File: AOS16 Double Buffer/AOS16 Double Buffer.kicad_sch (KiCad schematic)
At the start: 4 parts, among them IC1 SN74AUP2G14DCKR, J1 Conn_01x07_Pin, U1 74LS157, U2 74LS157

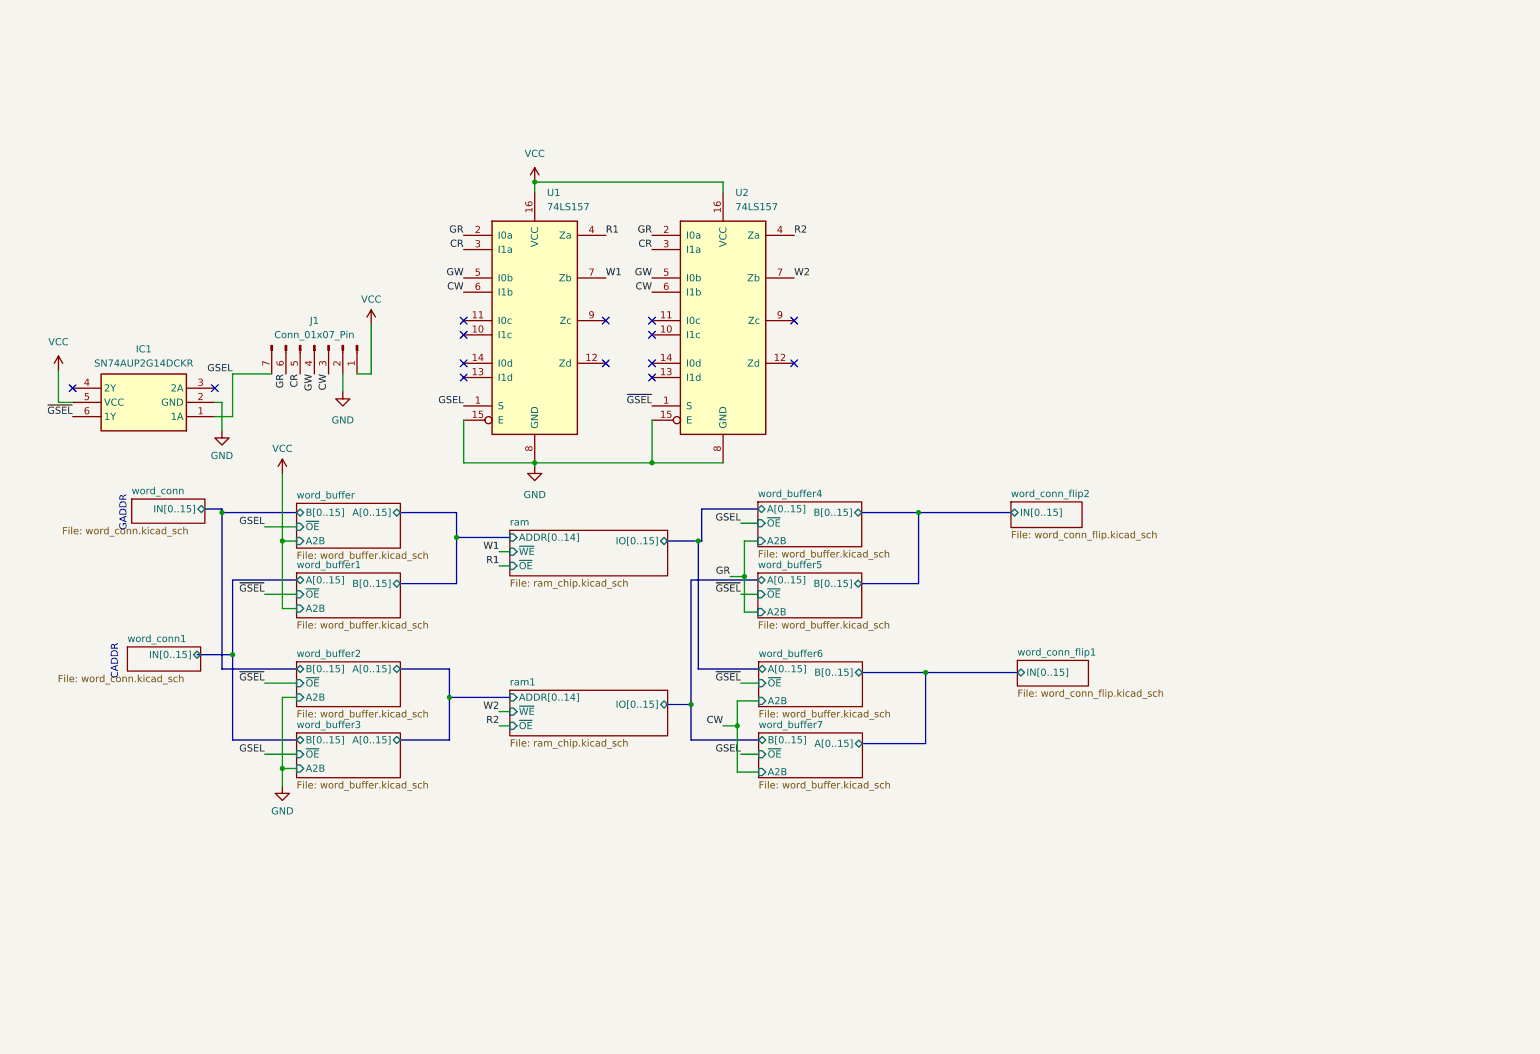
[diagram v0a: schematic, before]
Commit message: updated double buffer
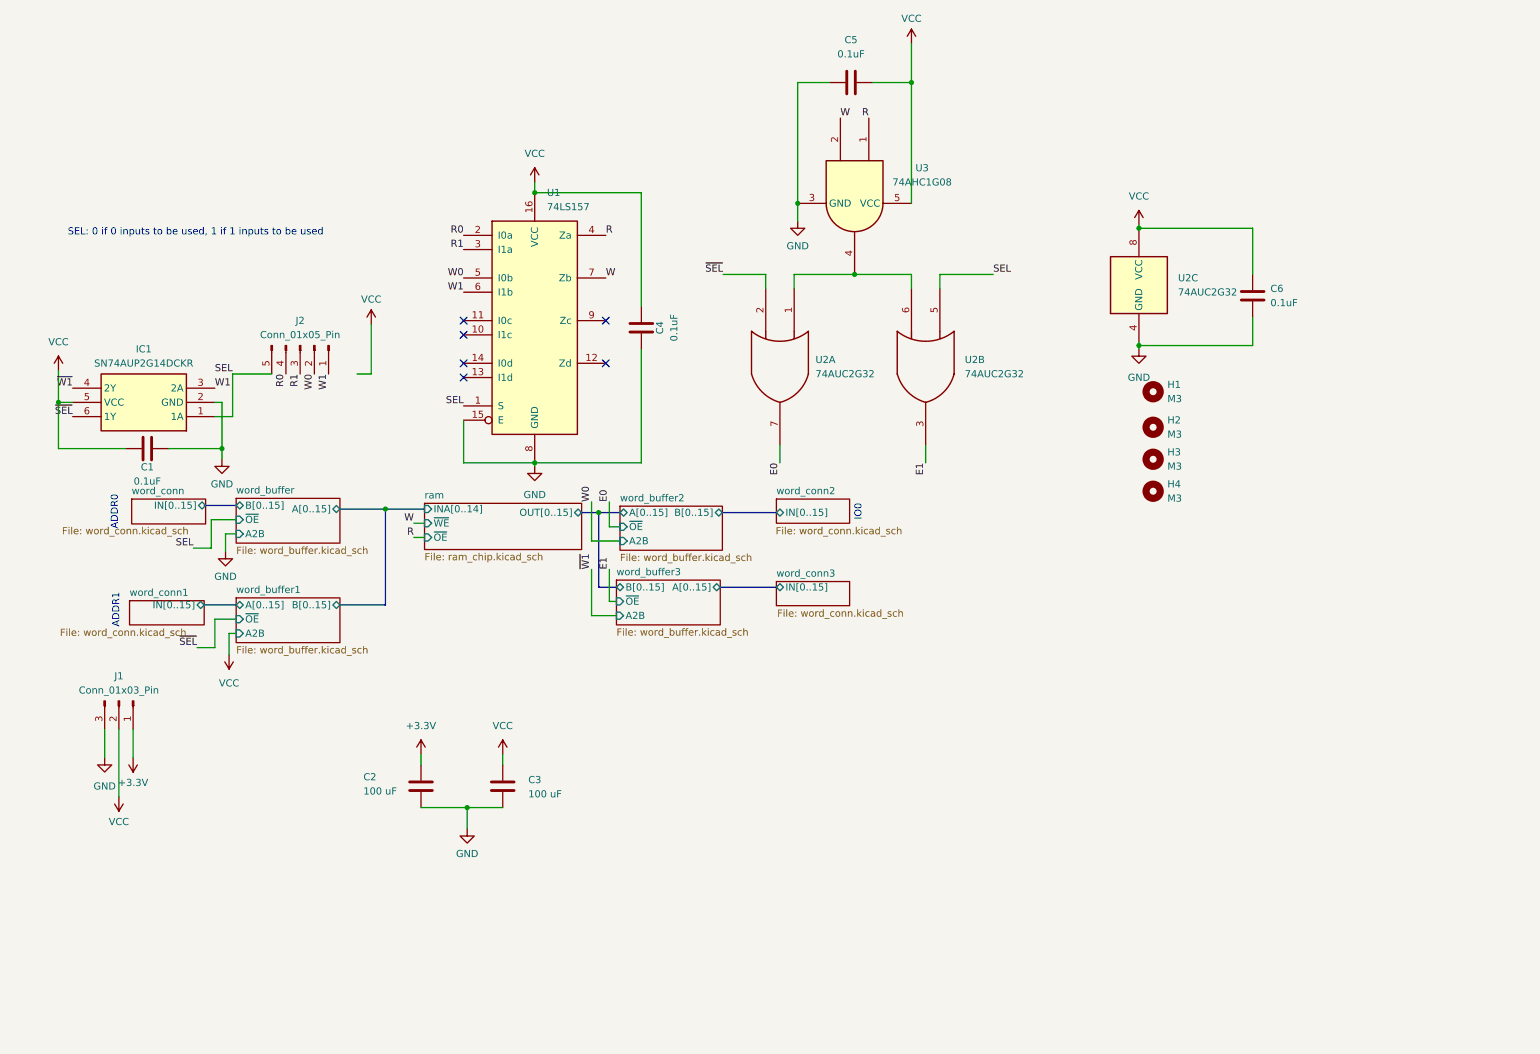
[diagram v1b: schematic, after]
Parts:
- removed J1: Conn_01x07_Pin, Connector_PinSocket_2.54mm:PinSocket_1x07_P2.54mm_Vertical, symbol Connector:Conn_01x07_Pin
- removed U2: 74LS157, Package_SO:SOIC-16_3.9x9.9mm_P1.27mm, symbol 74xx:74LS157
- added C1, C4, C5, C6: 0.1uF, Capacitor_SMD:C_0603_1608Metric, symbol Device:C
- added C2, C3: 100 uF, Capacitor_SMD:CP_Elec_5x5.3, symbol Device:C
- added H1, H2, H3, H4: M3, MountingHole:MountingHole_3.2mm_M3, symbol Mechanical:MountingHole
- added J1: Conn_01x03_Pin, Connector_PinHeader_2.54mm:PinHeader_1x03_P2.54mm_Vertical, symbol Connector:Conn_01x03_Pin
- added J2: Conn_01x05_Pin, Connector_PinHeader_2.54mm:PinHeader_1x05_P2.54mm_Vertical, symbol Connector:Conn_01x05_Pin
- added U2: 74AUC2G32, Package_SO:SSOP-8_2.95x2.8mm_P0.65mm, symbol 74xGxx:74AUC2G32
- added U3: 74AHC1G08, Package_TO_SOT_SMD:SOT-23-5, symbol 74xGxx:74AHC1G08
- IC1: footprint sn74aup2:SOT65P210X110-6N -> Package_TO_SOT_SMD:SOT-363_SC-70-6
- U1: Manufacturer_Part_Number (none) -> SN74LS157
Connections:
- net CR is gone; now on net R1: U1.3 (I1a)
- net CW is gone; now on net W1: U1.6 (I1b)
- net GND: now also C1.2, C2.2, C3.2, C4.1, C5.1, C6.2, J1.3 (Pin_3), U2.4 (GND), U3.3 (GND)
- net R1: now also J2.3 (Pin_3); no longer U1.4 (Za)
- net VCC: now also C1.1, C3.1, C4.2, C5.2, C6.1, J1.2 (Pin_2), U2.8 (VCC), U3.5 (VCC)
- net W1: now also IC1.3 (2A), J2.1 (Pin_1); no longer U1.7 (Zb)
- net ~{W1}: now reaches IC1.4 (2Y)
- net GR renamed R0
- net R0: now also J2.4 (Pin_4)
- net GSEL renamed SEL
- net SEL: now also J2.5 (Pin_5), U2.5
- net GW renamed W0
- net W0: now also J2.2 (Pin_2)
- net ~{GSEL} renamed ~{SEL}
- net ~{SEL}: now also U2.2
- new net: U2.1, U2.6, U3.4
- new net +3.3V: C2.1, J1.1 (Pin_1)
- new net E0: U2.7
- new net E1: U2.3
- new net R: U1.4 (Za), U3.1
- new net W: U1.7 (Zb), U3.2
- no-connect marks 14 -> 6
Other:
- removed sheet ram1
- removed sheet word_buffer4
- removed sheet word_buffer5
- removed sheet word_buffer6
- removed sheet word_buffer7
- removed sheet word_conn_flip1
- removed sheet word_conn_flip2
- added sheet word_conn2 (word_conn.kicad_sch)
- added sheet word_conn3 (word_conn.kicad_sch)
- sheet ram ports: added INA[0..14], OUT[0..15]; removed ADDR[0..14], IO[0..15]
- note added: "ADDR0"
- note added: "ADDR1"
- note added: "IO0"
- note added: "SEL: 0 if 0 inputs to be used, 1 if 1 inputs to be used"
- note removed: "CADDR"
- note removed: "GADDR"

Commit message: Completed double buffer first draft
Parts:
- removed C4: 0.1uF, Capacitor_SMD:C_0603_1608Metric, symbol Device:C
- removed H1, H2, H3, H4: M3, MountingHole:MountingHole_3.2mm_M3, symbol Mechanical:MountingHole
- removed IC1: SN74AUP2G14DCKR, Package_TO_SOT_SMD:SOT-363_SC-70-6, symbol SN74AUP2G14DCKR:SN74AUP2G14DCKR
- removed J1: Conn_01x03_Pin, Connector_PinHeader_2.54mm:PinHeader_1x03_P2.54mm_Vertical, symbol Connector:Conn_01x03_Pin
- removed J2: Conn_01x05_Pin, Connector_PinHeader_2.54mm:PinHeader_1x05_P2.54mm_Vertical, symbol Connector:Conn_01x05_Pin
- removed U1: 74LS157, Package_SO:SOIC-16_3.9x9.9mm_P1.27mm, symbol 74xx:74LS157
- removed U2: 74AUC2G32, Package_SO:SSOP-8_2.95x2.8mm_P0.65mm, symbol 74xGxx:74AUC2G32
- removed U3: 74AHC1G08, Package_TO_SOT_SMD:SOT-23-5, symbol 74xGxx:74AHC1G08
- added C2, C7, C8, C9: 0.1uF, Capacitor_SMD:C_0603_1608Metric, symbol Device:C
- added J1: Conn_01x02_Pin, Connector_PinHeader_2.54mm:PinHeader_1x02_P2.54mm_Vertical, symbol Connector:Conn_01x02_Pin
- added J6: Conn_01x07_Pin, Connector_PinHeader_2.54mm:PinHeader_1x07_P2.54mm_Vertical, symbol Connector:Conn_01x07_Pin
- added U1, U2: 74AHC1G08, Package_TO_SOT_SMD:SOT-353_SC-70-5, symbol 74xGxx:74AHC1G08
- added U3, U4: 74AHC1G32, Package_TO_SOT_SMD:SOT-353_SC-70-5, symbol 74xGxx:74AHC1G32
- added U5, U6: 74AHC1G04, Package_TO_SOT_SMD:SOT-353_SC-70-5, symbol 74xGxx:74AHC1G04
- added U7: 74LS157, Package_SO:SOIC-16_3.9x9.9mm_P1.27mm, symbol 74xx:74LS157
- C1, C5, C6: Manufacturer_Part_Number CL10B104KO8WPNL -> (none)
- renumbered C2 to C3, C3 to C4
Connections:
- net +3.3V: now also J1.1 (Pin_1)
- net E0: now also U3.4
- net E1: now also U4.4
- net GND: now also C5.2, C2.2, C7.2, C8.2, C9.2, J1.2 (Pin_2), J6.7 (Pin_7), U1.3 (GND), U2.3 (GND), U3.3 (GND), U4.3 (GND), U5.3 (GND), U6.3 (GND), U7.15 (E), U7.8 (GND); no longer C5.1
- net R: now also U7.4 (Za)
- net R0: now also J6.4 (Pin_4), U1.1, U7.2 (I0a)
- net R1: now also J6.3 (Pin_3), U2.1, U7.3 (I1a)
- net SEL: now also J6.5 (Pin_5), U3.2, U5.2, U7.1 (S)
- net VCC: now also C5.1, C2.1, C7.1, C8.1, C9.1, J6.6 (Pin_6), U1.5 (VCC), U2.5 (VCC), U3.5 (VCC), U4.5 (VCC), U5.5 (VCC), U6.5 (VCC), U7.16 (VCC); no longer C5.2
- net W: now also U7.7 (Zb)
- net W0: now also J6.2 (Pin_2), U1.2, U7.5 (I0b)
- net W1: now also J6.1 (Pin_1), U2.2, U6.2, U7.6 (I1b)
- net ~{SEL}: now also U4.2, U5.4
- net ~{W1}: now also U6.4
- new net: U2.4, U4.1
- new net: U1.4, U3.1
- no-connect marks 6 -> 0
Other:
- note added: "IO1"
- note removed: "SEL: 0 if 0 inputs to be used, 1 if 1 inputs to be used"

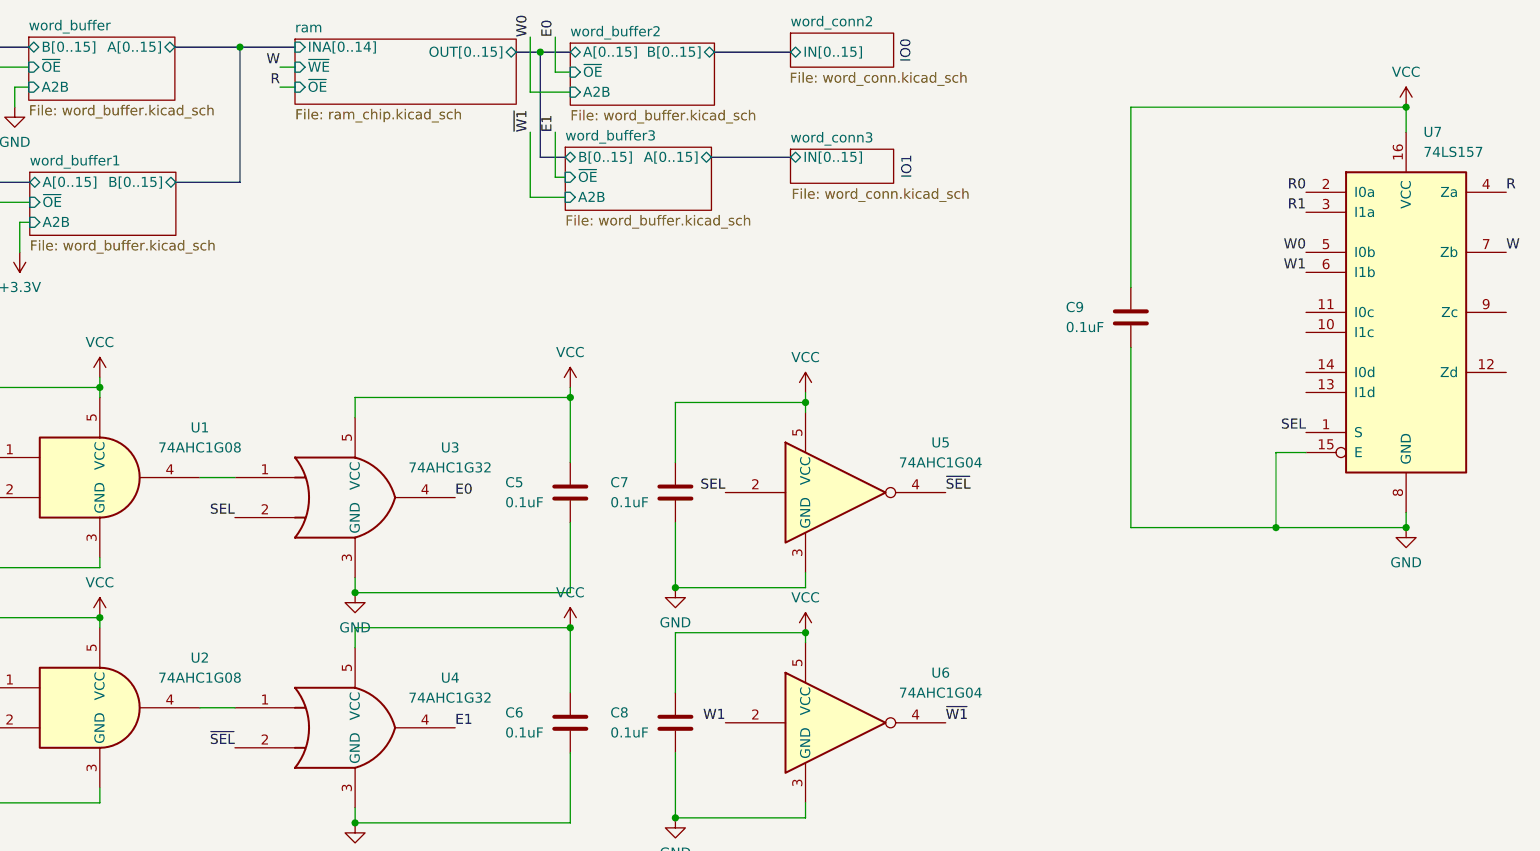
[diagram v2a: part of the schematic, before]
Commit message: Double Buffer Revision
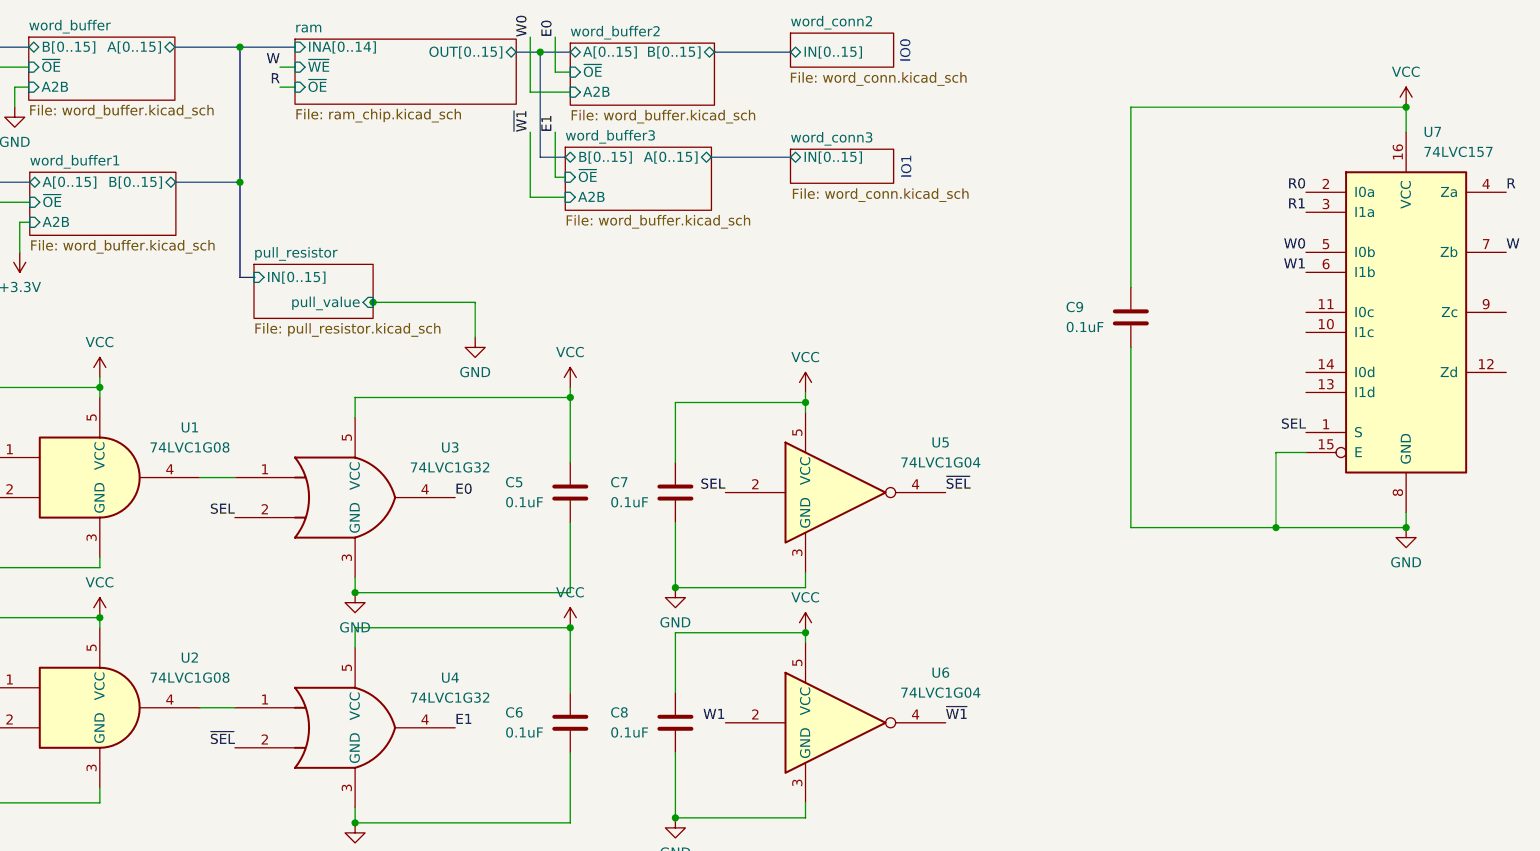
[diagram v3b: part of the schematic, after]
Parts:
- U1, U2: value 74AHC1G08 -> 74LVC1G08
- U3, U4: value 74AHC1G32 -> 74LVC1G32
- U5, U6: value 74AHC1G04 -> 74LVC1G04
- U7: value 74LS157 -> 74LVC157
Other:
- added sheet pull_resistor (pull_resistor.kicad_sch)
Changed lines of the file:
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@@
 	)
 	(junction
+		(at 90.551 53.34)
+		(diameter 0)
+		(color 0 0 0 0)
+	)
+	(junction
 		(at 32.385 86.995)
 		(diameter 0)
@@
 	)
 	(junction
+		(at 73.66 38.1)
+		(diameter 0)
+		(color 0 0 0 0)
+	)
+	(junction
 		(at 111.76 21.59)
 		(diameter 0)
@@
 		)
 	)
+	(bus
+		(pts
+			(xy 73.66 38.1) (xy 73.66 50.165)
+		)
+		(stroke
+			(width 0)
+			(type default)
+		)
+	)
 	(wire
 		(pts
@@
 	(wire
 		(pts
+			(xy 103.505 53.34) (xy 103.505 57.785)
+		)
+		(stroke
+			(width 0)
+			(type default)
+		)
+	)
+	(wire
+		(pts
 			(xy 186.69 59.055) (xy 186.69 81.915)
 		)
@@
 	(wire
 		(pts
+			(xy 90.17 53.34) (xy 90.551 53.34)
+		)
+		(stroke
+			(width 0)
+			(type default)
+		)
+	)
+	(wire
+		(pts
 			(xy 68.58 75.565) (xy 73.025 75.565)
 		)
@@
 		)
 	)
+	(bus
+		(pts
+			(xy 75.565 50.165) (xy 73.66 50.165)
+		)
+		(stroke
+			(width 0)
+			(type default)
+		)
+	)
 	(wire
 		(pts
@@
 	(wire
 		(pts
+			(xy 90.551 53.34) (xy 103.505 53.34)
+		)
+		(stroke
+			(width 0)
+			(type default)
+		)
+	)
+	(wire
+		(pts
 			(xy 55.88 86.995) (xy 55.88 85.725)
 		)
@@
 			)
 		)
-		(property "Value" "74AHC1G32"
+		(property "Value" "74LVC1G32"
 			(at 100.33 103.5364 0)
 			(effects
@@
 			)
 		)
-		(property "Value" "74AHC1G32"
+		(property "Value" "74LVC1G32"
 			(at 100.33 74.3264 0)
 			(effects
@@
 			)
 		)
-		(property "Value" "74LS157"
+		(property "Value" "74LVC157"
 			(at 223.8091 34.29 0)
 			(effects
@@
 			)
 		)
-		(property "Value" "74AHC1G04"
+		(property "Value" "74LVC1G04"
 			(at 162.56 73.6914 0)
 			(effects
@@
 	)
 	(symbol
+		(lib_id "power:GND")
+		(at 103.505 57.785 0)
+		(unit 1)
+		(exclude_from_sim no)
+		(in_bom yes)
+		(on_board yes)
+		(dnp no)
+		(fields_autoplaced yes)
+		(property "Reference" "#PWR042"
+			(at 103.505 64.135 0)
+			(effects
+				(font
+					(size 1.27 1.27)
+				)
+				(hide yes)
+			)
+		)
+		(property "Value" "GND"
+			(at 103.505 62.23 0)
+			(effects
+				(font
+					(size 1.27 1.27)
+				)
+			)
+		)
+		(property "Footprint" ""
+			(at 103.505 57.785 0)
+			(effects
+				(font
+					(size 1.27 1.27)
+				)
+				(hide yes)
+			)
+		)
+		(property "Datasheet" ""
+			(at 103.505 57.785 0)
+			(effects
+				(font
+					(size 1.27 1.27)
+				)
+				(hide yes)
+			)
+		)
+		(property "Description" "Power symbol creates a global label with name \"GND\" , ground"
+			(at 103.505 57.785 0)
+			(effects
+				(font
+					(size 1.27 1.27)
+				)
+				(hide yes)
+			)
+		)
+		(pin "1"
+		)
+		(instances
+			(project ""
+				(path "/131fc824-3141-4c3d-90f1-eeaffe39dfa6"
+					(reference "#PWR042")
+					(unit 1)
+				)
+			)
+		)
+	)
+	(symbol
 		(lib_id "power:VCC")
 		(at 145.415 64.77 0)
@@
 		(fields_autoplaced yes)
 		(property "Reference" "U2"
-			(at 68.58 98.4564 0)
+			(at 67.31 98.4564 0)
 			(effects
 				(font
@@
 			)
 		)
-		(property "Value" "74AHC1G08"
-			(at 68.58 100.9964 0)
+		(property "Value" "74LVC1G08"
+			(at 67.31 100.9964 0)
 			(effects
 				(font
@@
 		(fields_autoplaced yes)
 		(property "Reference" "U1"
-			(at 68.58 69.2464 0)
+			(at 67.31 69.2464 0)
 			(effects
 				(font
@@
 			)
 		)
-		(property "Value" "74AHC1G08"
-			(at 68.58 71.7864 0)
+		(property "Value" "74LVC1G08"
+			(at 67.31 71.7864 0)
 			(effects
 				(font
@@
 			)
 		)
-		(property "Value" "74AHC1G04"
+		(property "Value" "74LVC1G04"
 			(at 162.56 102.9014 0)
 			(effects
@@
 				)
 			)
+		)
+	)
+	(sheet
+		(at 75.438 48.514)
+		(size 15.113 6.858)
+		(fields_autoplaced yes)
+		(stroke
+			(width 0.1524)
+			(type solid)
+		)
+		(fill
+			(color 0 0 0 0.0000)
+		)
+		(property "Sheetname" "pull_resistor"
+			(at 75.438 47.8024 0)
+			(effects
+				(font
+					(size 1.27 1.27)
+				)
+				(justify left bottom)
+			)
+		)
+		(property "Sheetfile" "pull_resistor.kicad_sch"
+			(at 75.438 55.9566 0)
+			(effects
+				(font
+					(size 1.27 1.27)
+				)
+				(justify left top)
+			)
+		)
+		(pin "IN[0..15]" input
+			(at 75.438 50.165 180)
+			(effects
+				(font
+					(size 1.27 1.27)
+				)
+				(justify left)
+			)
+		)
+		(pin "pull_value" input
+			(at 90.551 53.34 0)
+			(effects
+				(font
+					(size 1.27 1.27)
+				)
+				(justify right)
+			)
+		)
+		(instances
+			(project "AOS16 Double Buffer"
+				(path "/131fc824-3141-4c3d-90f1-eeaffe39dfa6"
+					(page "11")
+				)
+			)
